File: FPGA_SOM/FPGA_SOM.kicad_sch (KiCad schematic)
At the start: 60 parts, among them J1 Conn_01x12, J2 Conn_02x05_Counter_Clockwise, J3 Conn_01x06, J5 Conn_01x02, J7 Conn_01x09, J8 Conn_01x10, SW1 SW_Push, U1 ICE40UP5K-SG48ITR, U101 W25X20CLSN, U2 AP2127N-3.3, U3 AP2127N-1.2, X101 ECS-2520MV-xxx-xx

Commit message: QOL changes before production.
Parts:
- removed D2, D3, D4: LED_Small, Diode_SMD:D_0603_1608Metric_Pad1.05x0.95mm_HandSolder, symbol Device:LED_Small
- removed TP5: FSS, TestPoint:TestPoint_THTPad_D2.0mm_Drill1.0mm, symbol Connector:TestPoint
- removed TP6: ISS, TestPoint:TestPoint_THTPad_D2.0mm_Drill1.0mm, symbol Connector:TestPoint
- added D1: LED_RAGB, LED_SMD:LED_SK6812_EC15_1.5x1.5mm, symbol Device:LED_RAGB
- added R108 (x3): 2k2, Resistor_SMD:R_0603_1608Metric, symbol Device:R
- C101, C107, C120, C126, C132, C133, C138: LCSC Part # (none) -> C14663
- C119, C134: footprint Capacitor_SMD:C_0805_2012Metric -> Capacitor_SMD:C_0603_1608Metric; LCSC Part # (none) -> C96446
- C122, C132: LCSC Part # (none) -> C19666
- C125, C131, C137: LCSC Part # (none) -> C15849
- C143: LCSC Part # (none) -> C57112
- FB1: footprint Resistor_SMD:R_1206_3216Metric -> Resistor_SMD:R_0603_1608Metric; LCSC Part # (none) -> C1002
- R102, R103: LCSC Part # (none) -> C25804
- R103: LCSC Part # (none) -> C21189
- R108: LCSC Part # (none) -> C22775
- R109, R112: LCSC Part # (none) -> C4190
- R113: LCSC Part # (none) -> C23162
- U1: LCSC Part # (none) -> C2678152
- U101: LCSC Part # (none) -> C97521
- X101: value ECS-2520MV-xxx-xx -> SX2M20.000B10F20TNN; LCSC Part # (none) -> C7431315
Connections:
- net 3V3: now also D1.2 (A)
- net RGB0: now also R108.1
- net RGB1: now also R108.1
- net RGB2: now also R108.1
- new net: D1.4 (BK), R108.2
- new net: D1.1 (RK), R108.2
- new net: D1.3 (GK), R108.2
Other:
- note added: "CMOS Crystal oscillator 24 MHz"
- note removed: "CMOS Crystal oscillator 20 MHz"
- note removed: "Don't need resistors as FPGA has programmable current sinks"
- moved on the sheet: C101, C122, U1A

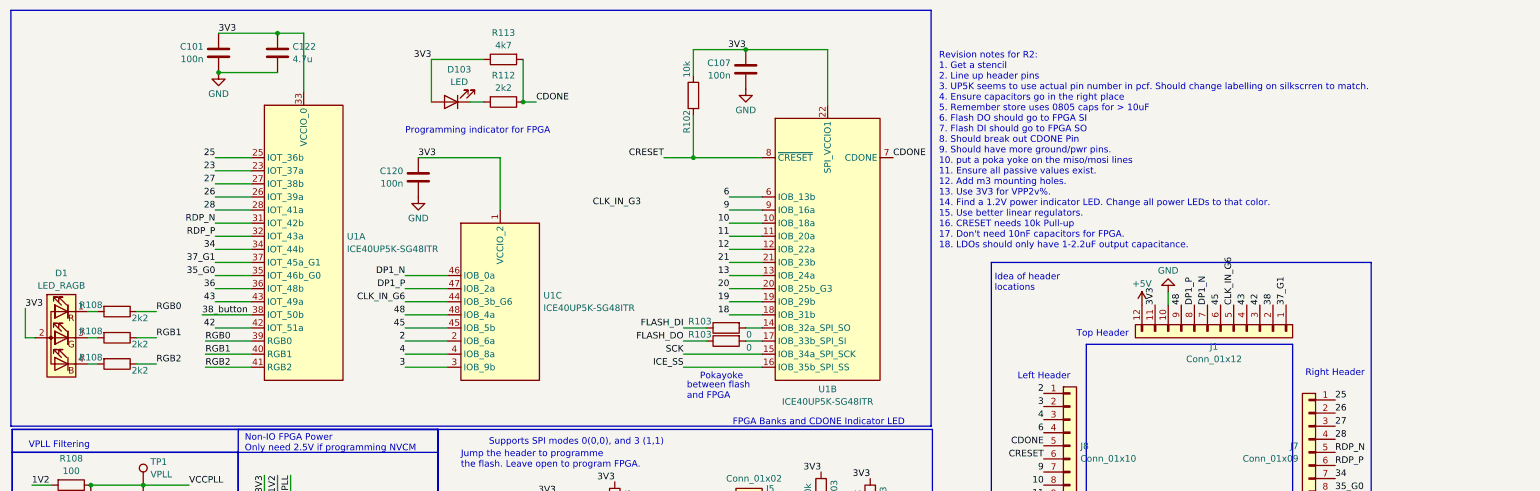
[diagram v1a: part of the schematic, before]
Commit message: Added notes to schematic.
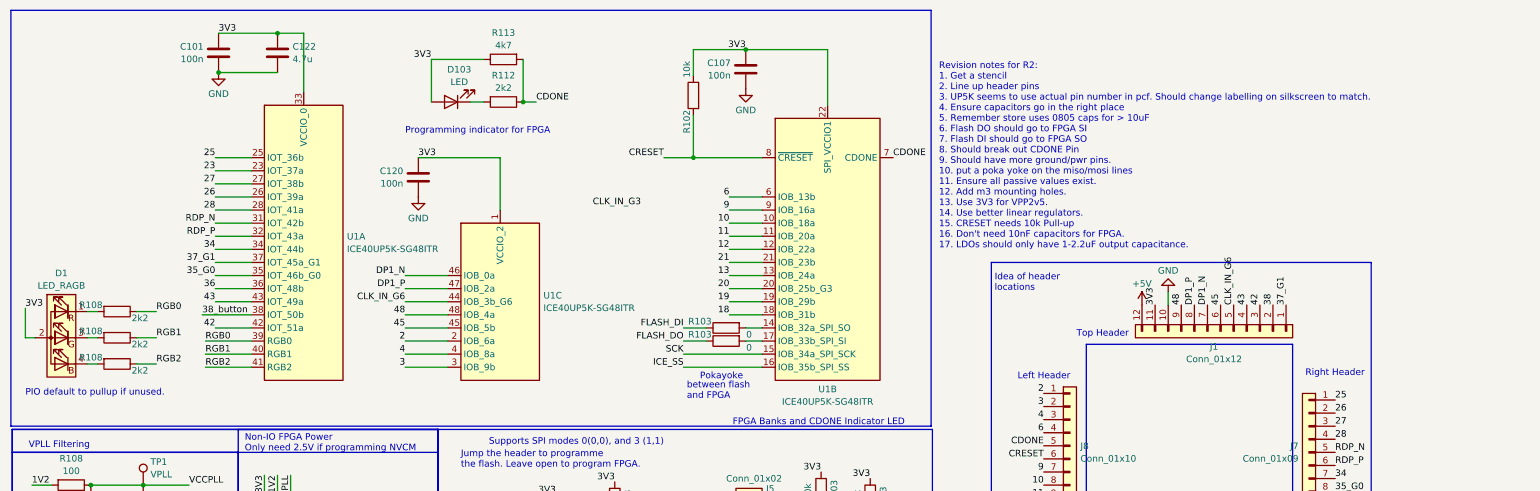
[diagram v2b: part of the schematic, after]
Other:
- note added: "PIO default to pullup if unused."
- note added: "Revision notes for R2: 1. Get a stencil 2. Line up header pins 3. UP5K seems to use actual pin number in pcf. Should change labelling on silkscreen to match. 4. Ensure capacitors go in the right place 5. Remember store uses 0805 caps for > 10uF 6. Flash DO should go to FPGA SI 7. Flash DI should go to FPGA SO 8. Should break out CDONE Pin 9. Should have more ground/pwr pins. 10. put a poka yoke o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"
- note removed: "Revision notes for R2: 1. Get a stencil 2. Line up header pins 3. UP5K seems to use actual pin number in pcf. Should change labelling on silkscrren to match. 4. Ensure capacitors go in the right place 5. Remember store uses 0805 caps for > 10uF 6. Flash DO should go to FPGA SI 7. Flash DI should go to FPGA SO 8. Should break out CDONE Pin 9. Should have more ground/pwr pins. 10. put a poka yoke o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"
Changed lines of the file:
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@@
+    (effects (font (size 1.27 1.27)) (justify left bottom))
+  )
+  (text "PIO default to pullup if unused." (at 15.875 86.995 0)
     (effects (font (size 1.27 1.27)) (justify left bottom))
   )
@@
     (effects (font (size 1.27 1.27)) (justify left bottom))
   )
-  (text "Revision notes for R2:\n1. Get a stencil\n2. Line up header pins\n3. UP5K seems to use actual pin number in pcf. Should change labelling on silkscrren to match.\n4. Ensure capacitors go in the right place\n5. Remember store uses 0805 caps for > 10uF\n6. Flash DO should go to FPGA SI\n7. Flash DI should go to FPGA SO\n8. Should break out CDONE Pin\n9. Should have more ground/pwr pins.\n10. put a poka yoke on the miso/mosi lines\n11. Ensure all passive values exist.\n12. Add m3 mounting holes.\n13. Use 3V3 for VPP2v%.\n14. Find a 1.2V power indicator LED. Change all power LEDs to that color.\n15. Use better linear regulators.\n16. CRESET needs 10k Pull-up\n17. Don't need 10nF capacitors for FPGA.\n18. LDOs should only have 1-2.2uF output capacitance. "
+  (text "Revision notes for R2:\n1. Get a stencil\n2. Line up header pins\n3. UP5K seems to use actual pin number in pcf. Should change labelling on silkscreen to match.\n4. Ensure capacitors go in the right place\n5. Remember store uses 0805 caps for > 10uF\n6. Flash DO should go to FPGA SI\n7. Flash DI should go to FPGA SO\n8. Should break out CDONE Pin\n9. Should have more ground/pwr pins.\n10. put a poka yoke on the miso/mosi lines\n11. Ensure all passive values exist.\n12. Add m3 mounting holes.\n13. Use 3V3 for VPP2v5.\n14. Use better linear regulators.\n15. CRESET needs 10k Pull-up\n16. Don't need 10nF capacitors for FPGA.\n17. LDOs should only have 1-2.2uF output capacitance. "
     (at 193.04 58.42 0)
     (effects (font (size 1.27 1.27)) (justify left bottom))

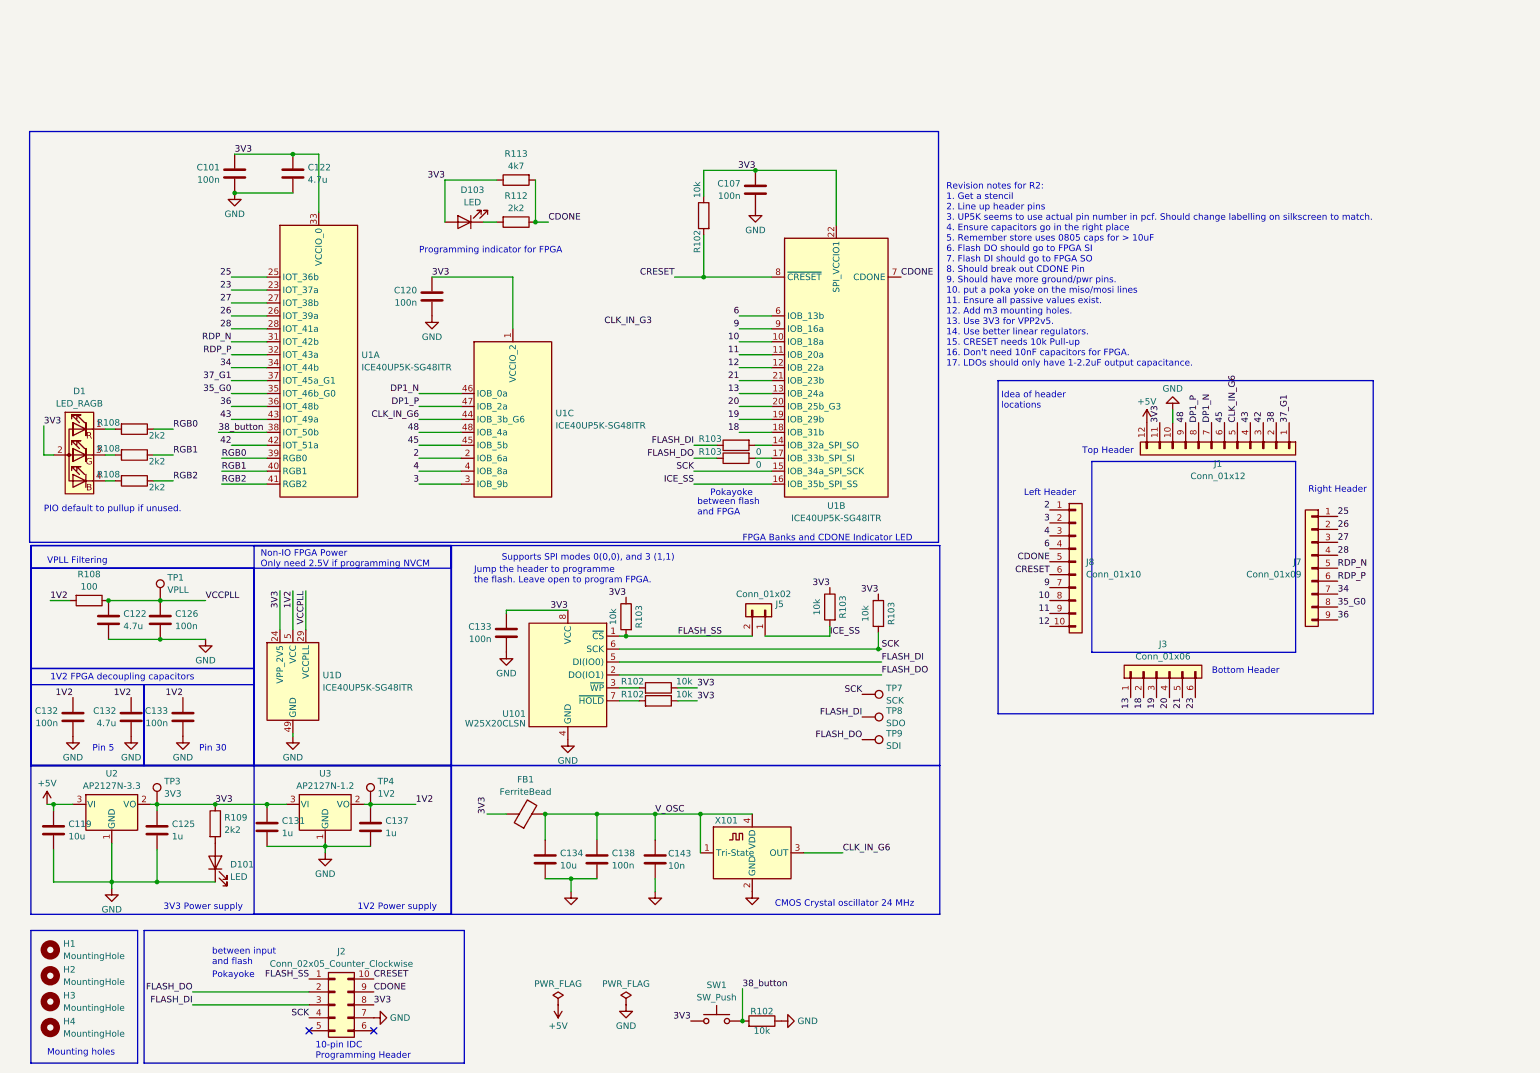
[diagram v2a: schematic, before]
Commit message: Added ethernet, usb-c, capacitive touch button, and PMOD to schematic. Started PCB layout for V3.
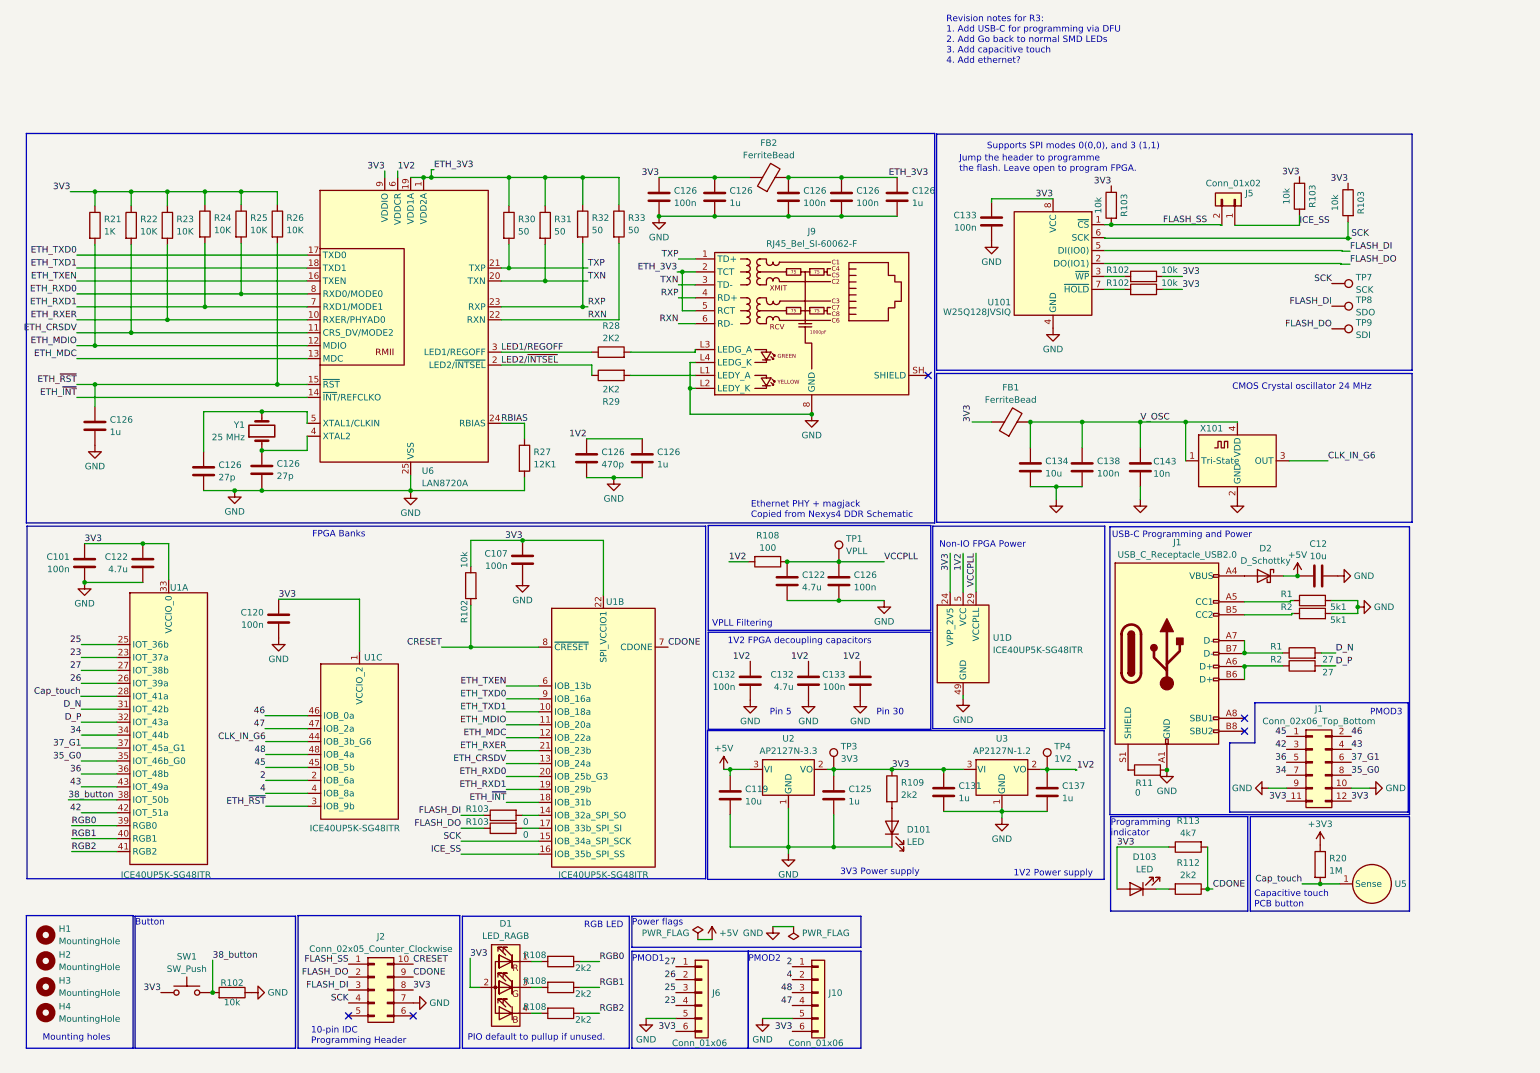
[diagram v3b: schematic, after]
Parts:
- removed J1: Conn_01x12, Connector_PinHeader_2.54mm:PinHeader_1x12_P2.54mm_Vertical, symbol Connector_Generic:Conn_01x12
- removed J3: Conn_01x06, Connector_PinHeader_2.54mm:PinHeader_1x06_P2.54mm_Vertical, symbol Connector_Generic:Conn_01x06
- removed J7: Conn_01x09, Connector_PinHeader_2.54mm:PinHeader_1x09_P2.54mm_Vertical, symbol Connector_Generic:Conn_01x09
- removed J8: Conn_01x10, Connector_PinHeader_2.54mm:PinHeader_1x10_P2.54mm_Vertical, symbol Connector_Generic:Conn_01x10
- added C12: 10u, Capacitor_SMD:C_0603_1608Metric, symbol Device:C
- added C126 (x2): 27p, Capacitor_SMD:C_0402_1005Metric, symbol Device:C
- added C126 (x3): 100n, Capacitor_SMD:C_0402_1005Metric, symbol Device:C
- added C126 (x4): 1u, Capacitor_SMD:C_0402_1005Metric, symbol Device:C
- added C126: 470p, Capacitor_SMD:C_0402_1005Metric, symbol Device:C
- added D2: D_Schottky, Diode_SMD:D_0603_1608Metric, symbol Device:D_Schottky
- added FB2: FerriteBead, Resistor_SMD:R_0603_1608Metric, symbol Device:FerriteBead
- added J1: Conn_02x06_Top_Bottom, Connector_PinHeader_2.54mm:PinHeader_2x06_P2.54mm_Horizontal, symbol Connector_Generic:Conn_02x06_Odd_Even
- added J1: USB_C_Receptacle_USB2.0, Connector_USB:USB_C_Receptacle_GCT_USB4105-xx-A_16P_TopMnt_Horizontal, symbol Connector:USB_C_Receptacle_USB2.0
- added J10, J6: Conn_01x06, Connector_PinHeader_2.54mm:PinHeader_1x06_P2.54mm_Horizontal, symbol Connector_Generic:Conn_01x06
- added J9: RJ45_Bel_SI-60062-F, Connector_RJ:RJ45_Bel_SI-60062-F, symbol Connector:RJ45_Bel_SI-60062-F
- added R1, R2: 5k1, Resistor_SMD:R_0402_1005Metric, symbol Device:R
- added R1, R2: 27, Resistor_SMD:R_0402_1005Metric, symbol Device:R
- added R11: 0, Resistor_SMD:R_0402_1005Metric, symbol Device:R
- added R20: 1M, Resistor_SMD:R_0603_1608Metric, symbol Device:R
- added R21: 1K, Resistor_SMD:R_0402_1005Metric, symbol Device:R
- added R22, R23, R24, R25, R26: 10K, Resistor_SMD:R_0402_1005Metric, symbol Device:R
- added R27: 12K1, Resistor_SMD:R_0402_1005Metric, symbol Device:R
- added R28, R29: 2K2, Resistor_SMD:R_0402_1005Metric, symbol Device:R
- added R30, R31, R32, R33: 50, Resistor_SMD:R_0402_1005Metric, symbol Device:R
- added U5: ~, ACustomFootprintLib:Capacitive_touchpad, symbol Sensor_Touch:Capacitive_touchpad
- added U6: LAN8720A, Package_DFN_QFN:VQFN-24-1EP_4x4mm_P0.5mm_EP2.5x2.5mm_ThermalVias, symbol Interface_Ethernet:LAN8720A
- added Y1: 25 MHz, Crystal:Crystal_SMD_2520-4Pin_2.5x2.0mm, symbol Device:Crystal
- C101, C107, C120, C125, C126, C131, C132, C133, C137, C138, C143: footprint Capacitor_SMD:C_0603_1608Metric -> Capacitor_SMD:C_0402_1005Metric
- R102, R103, R108, R109, R112, R113: footprint Resistor_SMD:R_0603_1608Metric -> Resistor_SMD:R_0402_1005Metric
- U101: value W25X20CLSN -> W25Q128JVSIQ
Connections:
- net +5V: now also C12.1, D2.1 (K)
- net 1V2: now also C126.1, C126.1, U6.6 (VDDCR)
- net 2: now also J10.1 (Pin_1)
- net 23: now also J6.4 (Pin_4)
- net 25: now also J6.3 (Pin_3)
- net 26: now also J6.2 (Pin_2)
- net 27: now also J6.1 (Pin_1)
- net 34: now also J1.7 (Pin_7)
- net 35_G0: now also J1.8 (Pin_8)
- net 36: now also J1.5 (Pin_5)
- net 37_G1: now also J1.6 (Pin_6)
- net 3V3: now also C126.1, C126.1, FB2.1, J1.11 (Pin_11), J1.12 (Pin_12), J10.6 (Pin_6), J6.6 (Pin_6), R21.1, R22.1, R23.1, R24.1, R25.1, R26.1, U6.9 (VDDIO)
- net 4: now also J10.2 (Pin_2)
- net 42: now also J1.3 (Pin_3)
- net 43: now also J1.4 (Pin_4)
- net 45: now also J1.1 (Pin_1)
- net 48: now also J10.3 (Pin_3)
- net GND: now also C12.2, C126.2, C126.2, C126.2, C126.2, C126.2, C126.2, C126.2, C126.2, C126.2, C126.2, J1.10 (Pin_10), J1.9 (Pin_9), J1.A1 (GND), J1.A12 (GND), J1.B1 (GND), J1.B12 (GND), J10.5 (Pin_5), J6.5 (Pin_5), J9.8 (GND), J9.L2 (LEDY_K), J9.L4 (LEDG_K), R1.2, R11.2, R2.2, R27.2, U6.25 (VSS)
- net 10 renamed ETH_TXD1
- net ETH_TXD1: now also U6.18 (TXD1)
- net 11 renamed ETH_MDIO
- net ETH_MDIO: now also R21.2, U6.12 (MDIO)
- net 12 renamed ETH_MDC
- net ETH_MDC: now also U6.13 (MDC)
- net 13 renamed ETH_CRSDV
- net ETH_CRSDV: now also R22.2, U6.11 (CRS_DV/MODE2)
- net 18 renamed ETH_~{INT}
- net ETH_~{INT}: now also U6.14 (~{INT}/REFCLKO)
- net 19 renamed ETH_RXD1
- net ETH_RXD1: now also R24.2, U6.7 (RXD1/MODE1)
- net 20 renamed ETH_RXD0
- net ETH_RXD0: now also R25.2, U6.8 (RXD0/MODE0)
- net 21 renamed ETH_RXER
- net ETH_RXER: now also R23.2, U6.10 (RXER/PHYAD0)
- net 28 renamed Cap_touch
- net Cap_touch: now also R20.2, U5.1 (Sense)
- net 3 renamed ETH_~{RST}
- net ETH_~{RST}: now also C126.1, R26.2, U6.15 (~{RST})
- net 6 renamed ETH_TXEN
- net ETH_TXEN: now also U6.16 (TXEN)
- net 9 renamed ETH_TXD0
- net ETH_TXD0: now also U6.17 (TXD0)
- net DP1_N renamed 46
- net 46: now also J1.2 (Pin_2)
- net DP1_P renamed 47
- net 47: now also J10.4 (Pin_4)
- net RDP_N renamed D_N
- net D_N: now also R1.2
- net RDP_P renamed D_P
- net D_P: now also R2.2
- new net: C126.1, U6.4 (XTAL2), Y1.1
- new net: J1.A5 (CC1), R1.1
- new net: C126.1, U6.5 (XTAL1/CLKIN), Y1.2
- new net: J1.S1 (SHIELD), R11.1
- new net: J1.B5 (CC2), R2.1
- new net: J9.L1 (LEDY_A), R29.2
- new net: J9.L3 (LEDG_A), R28.2
- new net: J1.A6 (D+), J1.B6 (D+), R2.1
- new net: D2.2 (A), J1.A4 (VBUS), J1.A9 (VBUS), J1.B4 (VBUS), J1.B9 (VBUS)
- new net: J1.A7 (D-), J1.B7 (D-), R1.1
- new net +3V3: R20.1
- new net ETH_3V3: C126.1, C126.1, C126.1, FB2.2, J9.2 (TCT), J9.5 (RCT), R30.1, R31.1, R32.1, R33.1, U6.1 (VDD2A), U6.19 (VDD1A)
- new net LED1/REGOFF: R28.1, U6.3 (LED1/REGOFF)
- new net LED2/~{INTSEL}: R29.1, U6.2 (LED2/~{INTSEL})
- new net RBIAS: R27.1, U6.24 (RBIAS)
- new net RXN: J9.6 (RD-), R33.2, U6.22 (RXN)
- new net RXP: J9.4 (RD+), R32.2, U6.23 (RXP)
- new net TXN: J9.3 (TD-), R31.2, U6.20 (TXN)
- new net TXP: J9.1 (TD+), R30.2, U6.21 (TXP)
- no-connect marks 2 -> 5
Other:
- note added: "Button"
- note added: "Capacitive touch PCB button"
- note added: "Ethernet PHY + magjack Copied from Nexys4 DDR Schematic"
- note added: "FPGA Banks"
- note added: "Non-IO FPGA Power"
- note added: "PMOD1"
- note added: "PMOD2"
- note added: "PMOD3"
- note added: "Power flags"
- note added: "Programming indicator"
- note added: "RGB LED"
- note added: "Revision notes for R3: 1. Add USB-C for programming via DFU 2. Add Go back to normal SMD LEDs 3. Add capacitive touch 4. Add ethernet?"
- note added: "USB-C Programming and Power"
- note removed: "Bottom Header"
- note removed: "FPGA Banks and CDONE Indicator LED"
- note removed: "Idea of header locations"
- note removed: "Left Header"
- note removed: "Non-IO FPGA Power Only need 2.5V if programming NVCM"
- note removed: "Pokayoke"
- note removed: "Programming indicator for FPGA"
- note removed: "Revision notes for R2: 1. Get a stencil 2. Line up header pins 3. UP5K seems to use actual pin number in pcf. Should change labelling on silkscreen to match. 4. Ensure capacitors go in the right place 5. Remember store uses 0805 caps for > 10uF 6. Flash DO should go to FPGA SI 7. Flash DI should go to FPGA SO 8. Should break out CDONE Pin 9. Should have more ground/pwr pins. 10. put a poka yoke o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"
- note removed: "Right Header"
- note removed: "Top Header"
- note removed: "between flash and FPGA"
- note removed: "between input and flash"
- moved on the sheet: C101, C107, C119, C120, C122, C125, C126, C131, C132, C133, C134, C137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
